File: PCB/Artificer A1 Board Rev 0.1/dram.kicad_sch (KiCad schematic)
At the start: 5 parts, among them U1 T527M00X0DCH, U14 K4UBE3D4AB-MGCL

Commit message: cleaned up, kicad 10 & usb c pd
migrated to Kicad 10,
added USB PD for power input
added capacitors inductors and resistor footprints
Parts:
- removed R63: 120R, symbol Device:R_Small
- removed R64, R65: 240R, symbol Device:R_Small
- added C100, C101, C102, C103, C104, C105, C106, C107, C108, C109, C110, C111, C112, C113, C114, C115, C116, C117, C118, C119, C120, C121, C122, C123, C124, C125, C126, C127, C128, C89, C90, C91, C92, C93, C94, C95, C96, C97, C98, C99: 100nF, PCM_JLCPCB:C_0402, symbol PCM_JLCPCB-Capacitors:0402,100nF,(2)
- added R39, R40: 240Ω, PCM_JLCPCB:R_0402, symbol PCM_JLCPCB-Resistors:0402,220Ω
- added R41: 120Ω, PCM_JLCPCB:R_0402, symbol PCM_JLCPCB-Resistors:0402,120Ω
- renumbered U14 to U12, U1 to U8
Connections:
- net GND: now also C100.2, C101.2, C102.2, C103.2, C104.2, C105.2, C106.2, C107.2, C108.2, C109.2, C110.2, C111.2, C112.2, C113.2, C114.2, C115.2, C116.2, C117.2, C118.2, C119.2, C120.2, C121.2, C122.2, C123.2, C124.2, C125.2, C126.2, C127.2, C128.2, C89.2, C90.2, C91.2, C92.2, C93.2, C94.2, C95.2, C96.2, C97.2, C98.2, C99.2
- net VDD06-DRAM: now also C100.1, C102.1, C104.1, C106.1, C108.1, C110.1, C112.1, C114.1, C116.1, C118.1, C120.1, C90.1, C92.1, C94.1, C96.1, C98.1, R39.1, R40.1, R41.2
- net VDD11-DRAM: now also C101.1, C103.1, C105.1, C107.1, C109.1, C111.1, C113.1, C115.1, C117.1, C119.1, C89.1, C91.1, C93.1, C95.1, C97.1, C99.1
- net VDD18-DRAM: now also C121.1, C122.1, C123.1, C124.1, C125.1, C126.1, C127.1, C128.1
- net at U12.A8 (ZQ1): now also R40.2
- net at U12.A5 (ZQ0): now also R39.2
- net at U8.AA29 (SZQ): now also R41.1
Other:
- moved on the sheet: U12A, U12B, U8E

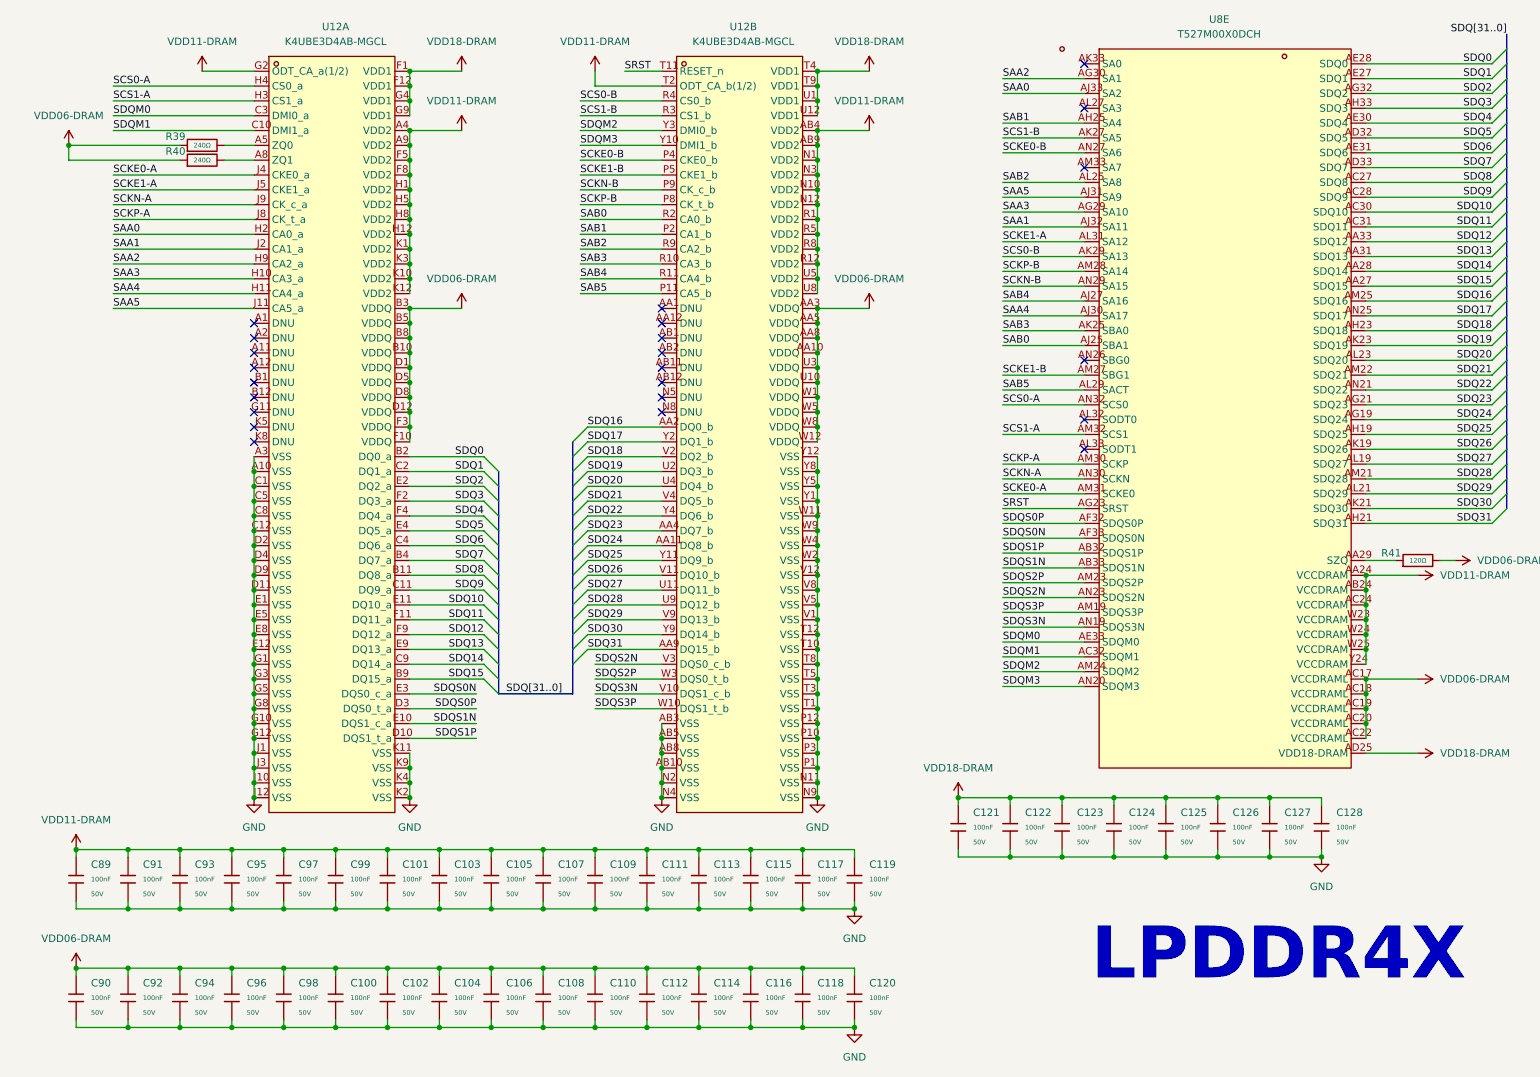
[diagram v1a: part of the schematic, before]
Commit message: placed all components
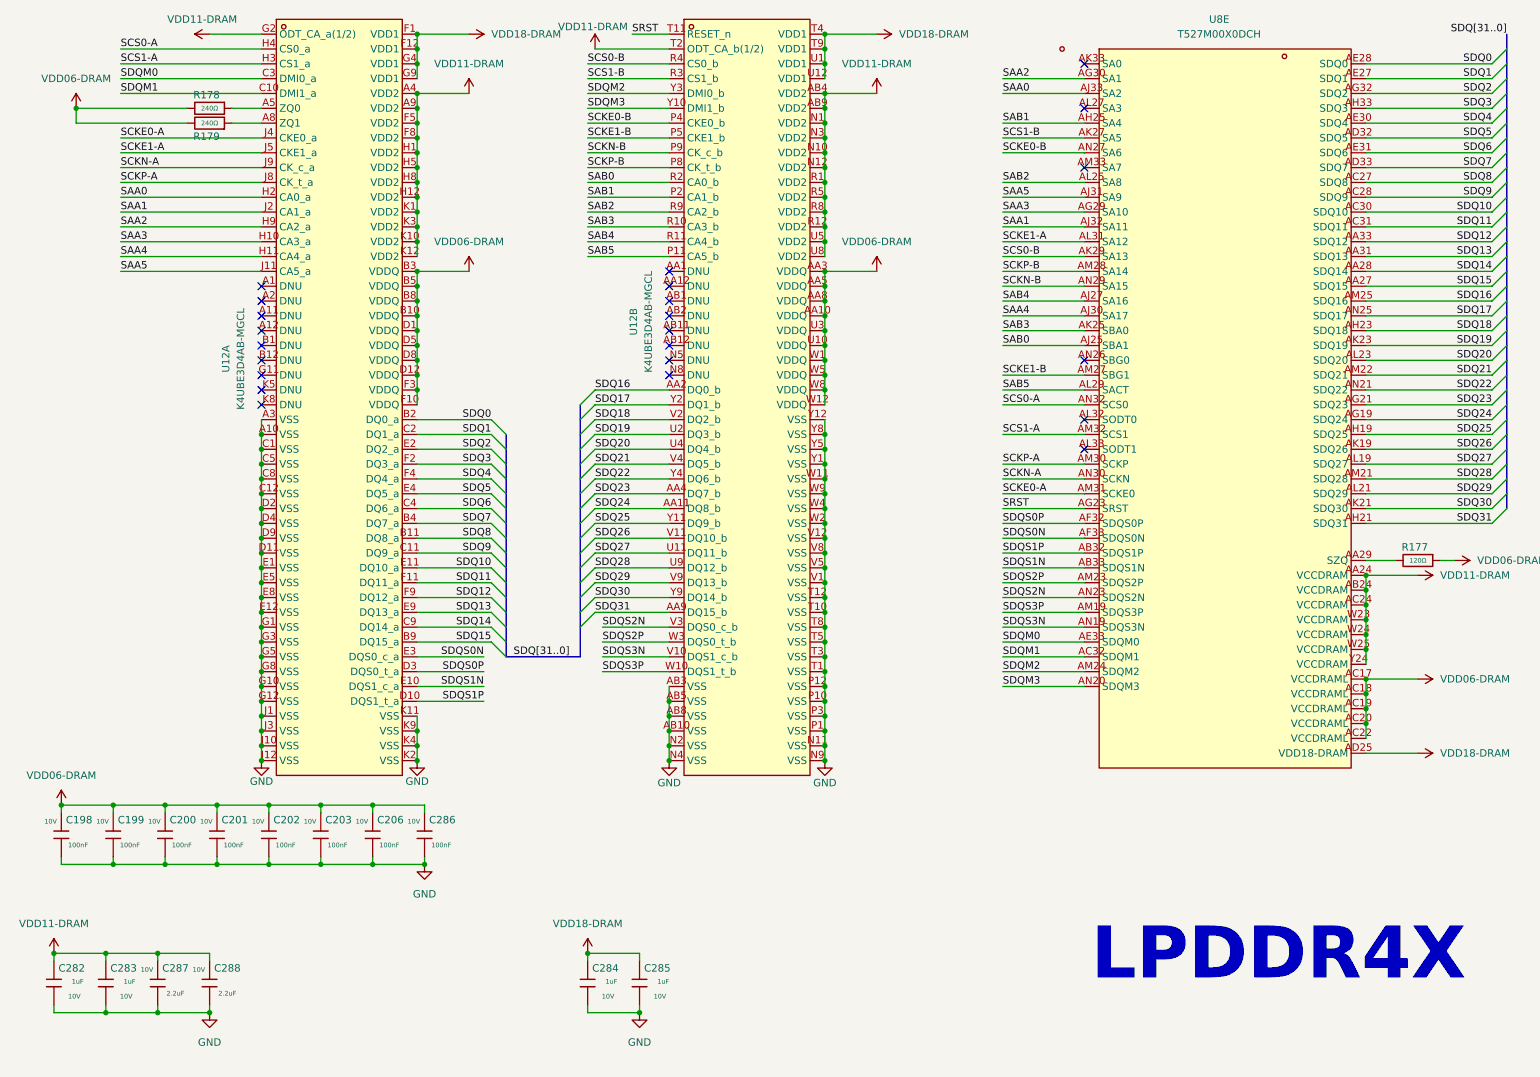
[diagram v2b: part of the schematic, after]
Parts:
- removed C100, C101, C102, C103, C104, C105, C106, C107, C108, C109, C110, C111, C112, C113, C114, C115, C116, C117, C118, C119, C120, C121, C122, C123, C124, C125, C126, C127, C128, C89, C90, C91, C92, C93, C94, C95, C96, C97, C98, C99: 100nF, PCM_JLCPCB:C_0402, symbol PCM_JLCPCB-Capacitors:0402,100nF,(2)
- removed R39, R40: 240Ω, PCM_JLCPCB:R_0402, symbol PCM_JLCPCB-Resistors:0402,220Ω
- removed R41: 120Ω, PCM_JLCPCB:R_0402, symbol PCM_JLCPCB-Resistors:0402,120Ω
- added C198, C199, C200, C201, C202, C203, C206, C286: 100nF, Capacitor_SMD:C_0201_0603Metric, symbol Cap:JLCPCB_Lib_Blank_Cap
- added C282, C283, C284, C285: 1uF, Capacitor_SMD:C_0201_0603Metric, symbol Cap:JLCPCB_Lib_Blank_Cap
- added C287, C288: 2.2uF, Capacitor_SMD:C_0201_0603Metric, symbol Cap:JLCPCB_Lib_Blank_Cap
- added R177: 120Ω, Resistor_SMD:R_0201_0603Metric, symbol Cap:JLCPCB_Res_Custom
- added R178, R179: 240Ω, Resistor_SMD:R_0201_0603Metric, symbol Cap:JLCPCB_Res_Custom
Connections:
- net GND: now also C198.1, C199.1, C200.1, C201.1, C202.1, C203.1, C206.1, C282.1, C283.1, C284.1, C285.1, C286.1, C287.1, C288.1
- net VDD06-DRAM: now also C198.2, C199.2, C200.2, C201.2, C202.2, C203.2, C206.2, C286.2, R177.1, R178.2, R179.2
- net VDD11-DRAM: now also C282.2, C283.2, C287.2, C288.2
- net VDD18-DRAM: now also C284.2, C285.2
- net at U12.A5 (ZQ0): now also R178.1
- net at U12.A8 (ZQ1): now also R179.1
- net at U8.AA29 (SZQ): now also R177.2
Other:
- moved on the sheet: U12A, U12B

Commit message: more routing and decoupling
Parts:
- removed C198, C199, C200, C201, C202, C203, C206, C286: 100nF, Capacitor_SMD:C_0201_0603Metric, symbol Cap:JLCPCB_Lib_Blank_Cap
- removed C282, C283, C284, C285: 1uF, Capacitor_SMD:C_0201_0603Metric, symbol Cap:JLCPCB_Lib_Blank_Cap
- added C308, C310, C311, C312, C313, C314, C315, C316, C317, C318, C319: 2.2uF, Capacitor_SMD:C_0201_0603Metric, symbol Cap:JLCPCB_Lib_Blank_Cap
- added C309, C320, C321, C322, C323: 100nF, Capacitor_SMD:C_0201_0603Metric, symbol Cap:JLCPCB_Lib_Blank_Cap
- added C324, C325: 10uF, Capacitor_SMD:C_0402_1005Metric, symbol Cap:JLCPCB_Lib_Blank_Cap
- C287, C288: Voltage Rated 10V -> 6.3V
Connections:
- net GND: now also C308.1, C309.1, C310.1, C311.1, C312.1, C313.1, C314.1, C315.1, C316.1, C317.1, C318.1, C319.1, C320.1, C321.1, C322.1, C323.1, C324.1, C325.1
- net VDD06-DRAM: now also C314.2, C315.2, C316.2, C317.2, C318.2, C319.2, C320.2, C321.2, C322.2, C323.2, C325.2
- net VDD11-DRAM: now also C310.2, C311.2, C312.2, C313.2, C324.2
- net VDD18-DRAM: now also C308.2, C309.2
- net SCKN-A renamed SCKA-N
- net SCKN-B renamed SCKB-N
- net SCKP-A renamed SCKA-P
- net SCKP-B renamed SCKB-P
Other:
- moved on the sheet: C287

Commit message: worked on power pours
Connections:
- net VDD18-DRAM: no longer C308.2, C309.2, U12.F1 (VDD1), U12.F12 (VDD1), U12.G4 (VDD1), U12.G9 (VDD1), U12.T4 (VDD1), U12.T9 (VDD1), U12.U1 (VDD1), U12.U12 (VDD1)
- new net VDD18-LPDDR: C308.2, C309.2, U12.F1 (VDD1), U12.F12 (VDD1), U12.G4 (VDD1), U12.G9 (VDD1), U12.T4 (VDD1), U12.T9 (VDD1), U12.U1 (VDD1), U12.U12 (VDD1)
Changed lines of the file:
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@@
 	)
 	(junction
-		(at 161.29 161.29)
-		(diameter 0)
-		(color 0 0 0 0)
-	)
-	(junction
 		(at 60.96 171.45)
 		(diameter 0)
@@
 	)
 	(junction
+		(at 161.29 161.29)
+		(diameter 0)
+		(color 0 0 0 0)
+	)
+	(junction
 		(at 57.15 102.87)
 		(diameter 0)
@@
 			)
 		)
-		(property "Value" "VDD18-DRAM"
+		(property "Value" "VDD18-LPDDR"
 			(at 96.52 16.5099 90)
 			(show_name no)
@@
 	)
 	(symbol
+		(lib_id "Power:VDD18-DRAM")
+		(at 161.29 161.29 0)
+		(unit 1)
+		(body_style 1)
+		(exclude_from_sim no)
+		(in_bom yes)
+		(on_board yes)
+		(in_pos_files yes)
+		(dnp no)
+		(fields_autoplaced yes)
+		(property "Reference" "#PWR0252"
+			(at 161.29 165.1 0)
+			(hide yes)
+			(show_name no)
+			(do_not_autoplace no)
+			(effects
+				(font
+					(size 1.27 1.27)
+				)
+			)
+		)
+		(property "Value" "VDD18-LPDDR"
+			(at 161.29 156.21 0)
+			(show_name no)
+			(do_not_autoplace no)
+			(effects
+				(font
+					(size 1.27 1.27)
+				)
+			)
+		)
+		(property "Footprint" ""
+			(at 161.29 161.29 0)
+			(hide yes)
+			(show_name no)
+			(do_not_autoplace no)
+			(effects
+				(font
+					(size 1.27 1.27)
+				)
+			)
+		)
+		(property "Datasheet" ""
+			(at 161.29 161.29 0)
+			(hide yes)
+			(show_name no)
+			(do_not_autoplace no)
+			(effects
+				(font
+					(size 1.27 1.27)
+				)
+			)
+		)
+		(property "Description" "Power symbol creates a global label with name \"VDD18-DRAM\""
+			(at 161.29 161.29 0)
+			(hide yes)
+			(show_name no)
+			(do_not_autoplace no)
+			(effects
+				(font
+					(size 1.27 1.27)
+				)
+			)
+		)
+		(pin "1"
+		)
+		(instances
+			(project "Artificer A1 Board Rev 0.1"
+				(path "/7c37bdb5-94b0-4567-b5ec-a879db855389/63456063-10c2-4b87-b70a-2f2a2a003610"
+					(reference "#PWR0252")
+					(unit 1)
+				)
+			)
+		)
+	)
+	(symbol
 		(lib_id "power:GND")
 		(at 33.02 190.5 0)
@@
 	)
 	(symbol
+		(lib_id "Power:VDD18-DRAM")
+		(at 162.56 16.51 270)
+		(unit 1)
+		(body_style 1)
+		(exclude_from_sim no)
+		(in_bom yes)
+		(on_board yes)
+		(in_pos_files yes)
+		(dnp no)
+		(fields_autoplaced yes)
+		(property "Reference" "#PWR0249"
+			(at 158.75 16.51 0)
+			(hide yes)
+			(show_name no)
+			(do_not_autoplace no)
+			(effects
+				(font
+					(size 1.27 1.27)
+				)
+			)
+		)
+		(property "Value" "VDD18-LPDDR"
+			(at 166.37 16.5099 90)
+			(show_name no)
+			(do_not_autoplace no)
+			(effects
+				(font
+					(size 1.27 1.27)
+				)
+				(justify left)
+			)
+		)
+		(property "Footprint" ""
+			(at 162.56 16.51 0)
+			(hide yes)
+			(show_name no)
+			(do_not_autoplace no)
+			(effects
+				(font
+					(size 1.27 1.27)
+				)
+			)
+		)
+		(property "Datasheet" ""
+			(at 162.56 16.51 0)
+			(hide yes)
+			(show_name no)
+			(do_not_autoplace no)
+			(effects
+				(font
+					(size 1.27 1.27)
+				)
+			)
+		)
+		(property "Description" "Power symbol creates a global label with name \"VDD18-DRAM\""
+			(at 162.56 16.51 0)
+			(hide yes)
+			(show_name no)
+			(do_not_autoplace no)
+			(effects
+				(font
+					(size 1.27 1.27)
+				)
+			)
+		)
+		(pin "1"
+		)
+		(instances
+			(project "Artificer A1 Board Rev 0.1"
+				(path "/7c37bdb5-94b0-4567-b5ec-a879db855389/63456063-10c2-4b87-b70a-2f2a2a003610"
+					(reference "#PWR0249")
+					(unit 1)
+				)
+			)
+		)
+	)
+	(symbol
 		(lib_id "Cap:JLCPCB_Res_Custom")
 		(at 48.26 29.21 270)
@@
 	)
 	(symbol
-		(lib_id "Power:VDD18-DRAM")
-		(at 162.56 16.51 270)
-		(unit 1)
-		(body_style 1)
-		(exclude_from_sim no)
-		(in_bom yes)
-		(on_board yes)
-		(in_pos_files yes)
-		(dnp no)
-		(fields_autoplaced yes)
-		(property "Reference" "#PWR0249"
-			(at 158.75 16.51 0)
-			(hide yes)
-			(show_name no)
-			(do_not_autoplace no)
-			(effects
-				(font
-					(size 1.27 1.27)
-				)
-			)
-		)
-		(property "Value" "VDD18-DRAM"
-			(at 166.37 16.5099 90)
-			(show_name no)
-			(do_not_autoplace no)
-			(effects
-				(font
-					(size 1.27 1.27)
-				)
-				(justify left)
-			)
-		)
-		(property "Footprint" ""
-			(at 162.56 16.51 0)
-			(hide yes)
-			(show_name no)
-			(do_not_autoplace no)
-			(effects
-				(font
-					(size 1.27 1.27)
-				)
-			)
-		)
-		(property "Datasheet" ""
-			(at 162.56 16.51 0)
-			(hide yes)
-			(show_name no)
-			(do_not_autoplace no)
-			(effects
-				(font
-					(size 1.27 1.27)
-				)
-			)
-		)
-		(property "Description" "Power symbol creates a global label with name \"VDD18-DRAM\""
-			(at 162.56 16.51 0)
-			(hide yes)
-			(show_name no)
-			(do_not_autoplace no)
-			(effects
-				(font
-					(size 1.27 1.27)
-				)
-			)
-		)
-		(pin "1"
-		)
-		(instances
-			(project "Artificer A1 Board Rev 0.1"
-				(path "/7c37bdb5-94b0-4567-b5ec-a879db855389/63456063-10c2-4b87-b70a-2f2a2a003610"
-					(reference "#PWR0249")
-					(unit 1)
-				)
-			)
-		)
-	)
-	(symbol
 		(lib_id "Power:VDD06-DRAM")
 		(at 52.07 180.34 0)
@@
 					(unit 1)
 				)
-			)
-		)
-	)
-	(symbol
-		(lib_id "Power:VDD18-DRAM")
-		(at 161.29 161.29 0)
-		(unit 1)
-		(body_style 1)
-		(exclude_from_sim no)
-		(in_bom yes)
-		(on_board yes)
-		(in_pos_files yes)
-		(dnp no)
-		(fields_autoplaced yes)
-		(property "Reference" "#PWR0252"
-			(at 161.29 165.1 0)
-			(hide yes)
-			(show_name no)
-			(do_not_autoplace no)
-			(effects
-				(font
-					(size 1.27 1.27)
-				)
-			)
-		)
-		(property "Value" "VDD18-DRAM"
-			(at 161.29 156.21 0)
-			(show_name no)
-			(do_not_autoplace no)
-			(effects
-				(font
-					(size 1.27 1.27)
-				)
-			)
-		)
-		(property "Footprint" ""
-			(at 161.29 161.29 0)
-			(hide yes)
-			(show_name no)
-			(do_not_autoplace no)
-			(effects
-				(font
-					(size 1.27 1.27)
-				)
-			)
-		)
-		(property "Datasheet" ""
-			(at 161.29 161.29 0)
-			(hide yes)
-			(show_name no)
-			(do_not_autoplace no)
-			(effects
-				(font
-					(size 1.27 1.27)
-				)
-			)
-		)
-		(property "Description" "Power symbol creates a global label with name \"VDD18-DRAM\""
-			(at 161.29 161.29 0)
-			(hide yes)
-			(show_name no)
-			(do_not_autoplace no)
-			(effects
-				(font
-					(size 1.27 1.27)
-				)
-			)
-		)
-		(pin "1"
-		)
-		(instances
-			(project "Artificer A1 Board Rev 0.1"
-				(path "/7c37bdb5-94b0-4567-b5ec-a879db855389/63456063-10c2-4b87-b70a-2f2a2a003610"
-					(reference "#PWR0252")
-					(unit 1)
-				)
